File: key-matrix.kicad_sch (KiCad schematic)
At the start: 210 parts, among them SW1 esc, SW10 f9, SW100 R ctrl, SW101 Left, SW102 down, SW103 right, SW104 num zero, SW105 num full stop, SW11 f10, SW12 f11, SW13 f12, SW14 prtscr, SW15 scrlck, SW16 pause, SW17 tilde, SW18 1, SW19 2, SW2 f1, SW20 3, SW21 4, SW22 5, SW23 6, SW24 7, SW25 8, SW26 9, SW27 0, SW28 minus, SW29 equals, SW3 f2, SW30 backspace, SW31 insert, SW32 home, SW33 pgup, SW34 num lock, SW35 num slash, SW36 num mult, SW37 num minus, SW38 tab, SW39 q, SW4 f3, SW40 w, SW41 e, SW42 r, SW43 t, SW44 y, SW45 u, SW46 i, SW47 o, SW48 p, SW49 L brac, SW5 f4, SW50 R brac, SW51 enter, SW52 delete, SW53 end, SW54 pgdn, SW55 num 7, SW56 num 8, SW57 num 9, SW58 num add, SW59 capslock, SW6 f5, SW60 a, SW61 s, SW62 d, SW63 f, SW64 g, SW65 h, SW66 j, SW67 k, SW68 l, SW69 sem colon, SW7 f6, SW70 quote, SW71 tilde, SW72 num 4, SW73 num 5, SW74 num 6, SW75 L shift, SW76 backslash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

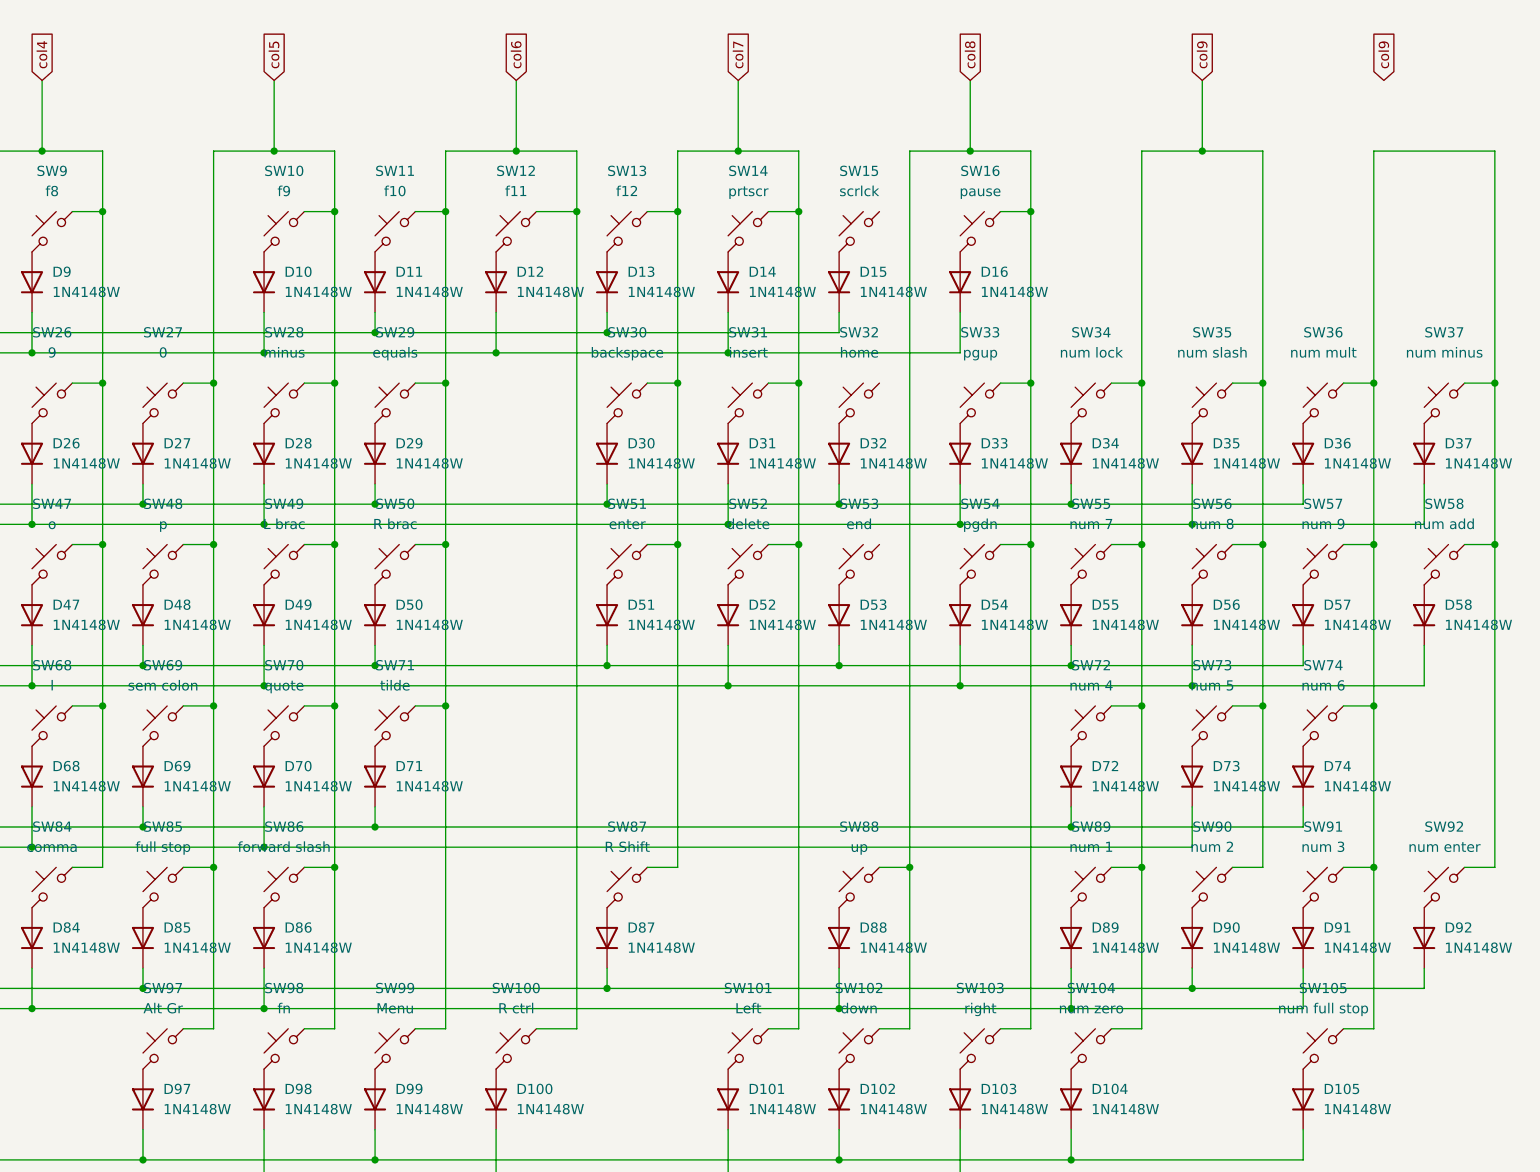
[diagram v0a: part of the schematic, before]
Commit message: Fixed key matrix, laid out LED matrix, started laying out microcontroller
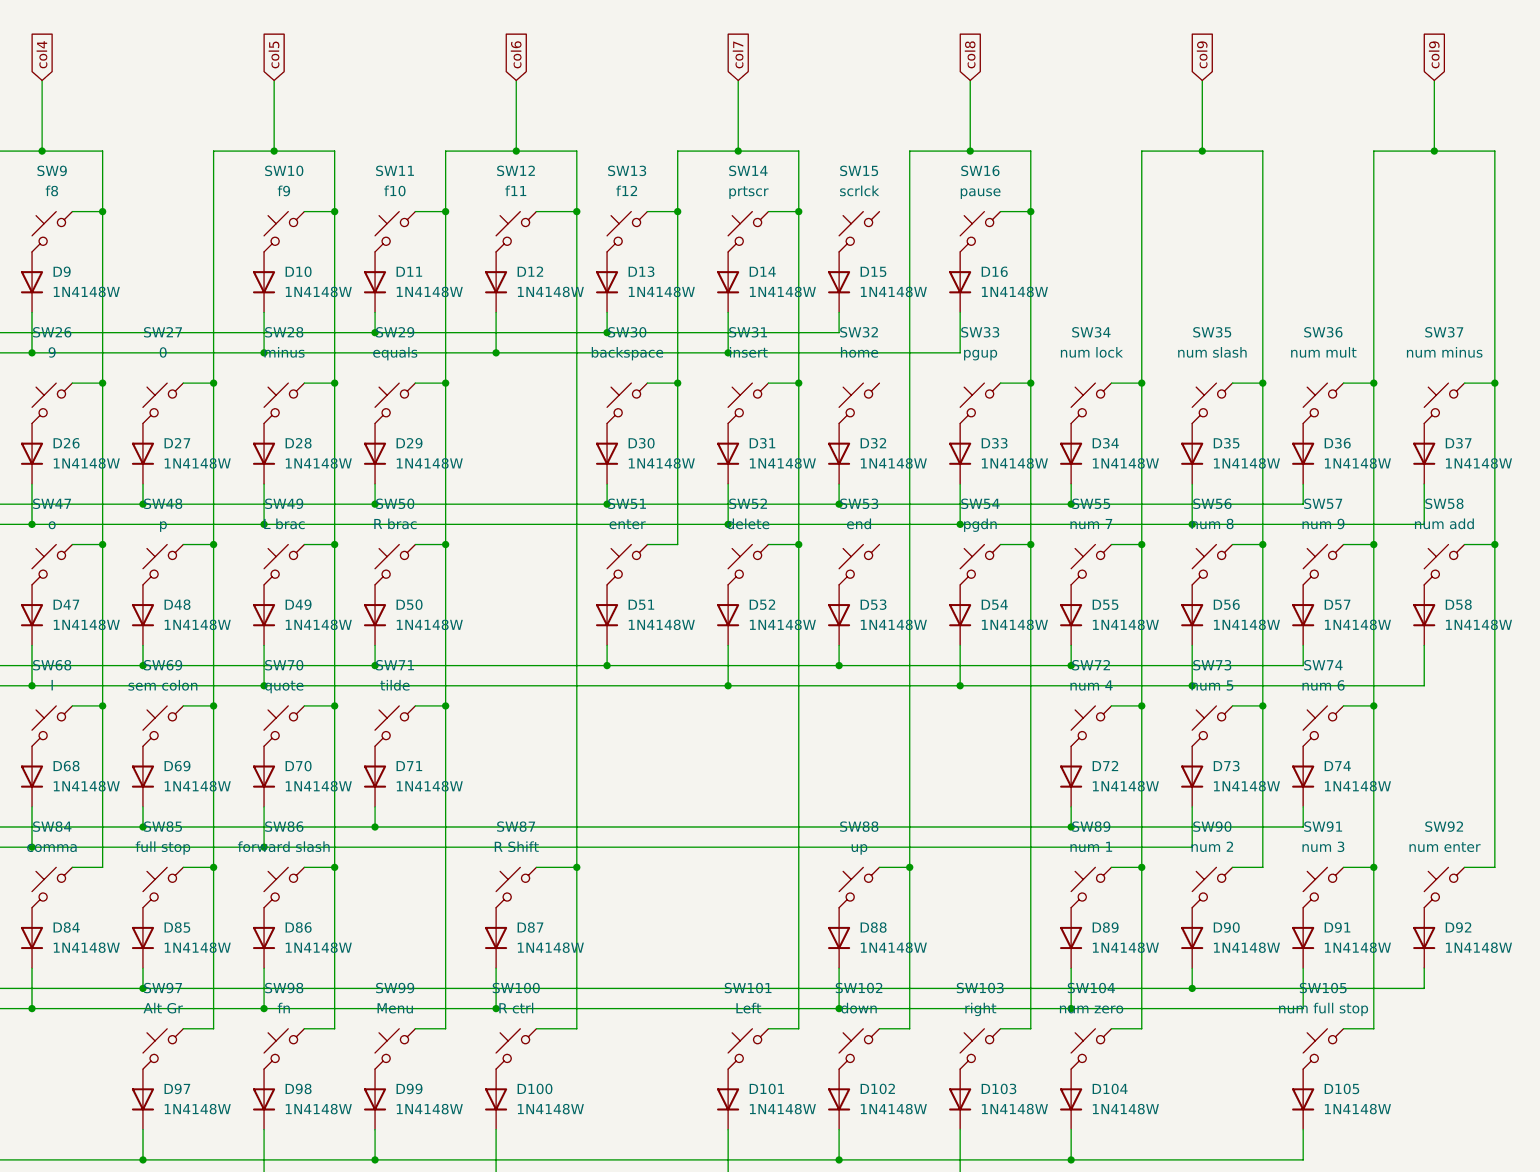
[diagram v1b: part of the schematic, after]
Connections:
- net col6: now also SW87.1
- net col7: no longer SW87.1
- net col9: now also SW105.1, SW36.1, SW37.1, SW57.1, SW58.1, SW74.1, SW91.1, SW92.1
- net row8: no longer D87.1 (K)
- net row9: now also D87.1 (K)
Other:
- moved on the sheet: D87, SW87
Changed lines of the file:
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@@
 	)
 	(junction
+		(at 257.81 134.62)
+		(diameter 0)
+		(color 0 0 0 0)
+	)
+	(junction
 		(at 139.7 114.3)
 		(diameter 0)
@@
 	)
 	(junction
-		(at 270.51 93.98)
+		(at 250.19 44.45)
 		(diameter 0)
 		(color 0 0 0 0)
 	)
 	(junction
-		(at 250.19 44.45)
+		(at 365.76 44.45)
 		(diameter 0)
 		(color 0 0 0 0)
@@
 	)
 	(junction
-		(at 261.62 149.86)
-		(diameter 0)
-		(color 0 0 0 0)
-	)
-	(junction
 		(at 320.04 109.22)
 		(diameter 0)
@@
 	)
 	(junction
+		(at 247.65 152.4)
+		(diameter 0)
+		(color 0 0 0 0)
+	)
+	(junction
 		(at 314.96 93.98)
 		(diameter 0)
@@
 	(wire
 		(pts
-			(xy 266.7 134.62) (xy 270.51 134.62)
-		)
-		(stroke
-			(width 0)
-			(type default)
-		)
-	)
-	(wire
-		(pts
 			(xy 124.46 93.98) (xy 124.46 73.66)
 		)
@@
 	(wire
 		(pts
-			(xy 257.81 52.07) (xy 257.81 154.94)
+			(xy 257.81 52.07) (xy 257.81 134.62)
 		)
 		(stroke
@@
 	(wire
 		(pts
-			(xy 261.62 149.86) (xy 335.28 149.86)
+			(xy 257.81 44.45) (xy 257.81 52.07)
 		)
 		(stroke
@@
 	(wire
 		(pts
-			(xy 257.81 44.45) (xy 257.81 52.07)
+			(xy 369.57 93.98) (xy 373.38 93.98)
 		)
 		(stroke
@@
 	(wire
 		(pts
-			(xy 369.57 93.98) (xy 373.38 93.98)
+			(xy 276.86 64.77) (xy 276.86 69.85)
 		)
 		(stroke
@@
 	(wire
 		(pts
-			(xy 276.86 64.77) (xy 276.86 69.85)
+			(xy 173.99 149.86) (xy 203.2 149.86)
 		)
 		(stroke
@@
 	(wire
 		(pts
-			(xy 173.99 149.86) (xy 203.2 149.86)
+			(xy 144.78 67.31) (xy 173.99 67.31)
 		)
 		(stroke
@@
 	(wire
 		(pts
-			(xy 144.78 67.31) (xy 173.99 67.31)
+			(xy 139.7 93.98) (xy 139.7 114.3)
 		)
 		(stroke
@@
 	(wire
 		(pts
-			(xy 139.7 93.98) (xy 139.7 114.3)
+			(xy 86.36 109.22) (xy 86.36 106.68)
 		)
 		(stroke
@@
 	(wire
 		(pts
-			(xy 86.36 109.22) (xy 86.36 106.68)
+			(xy 365.76 44.45) (xy 373.38 44.45)
 		)
 		(stroke
@@
 	(wire
 		(pts
-			(xy 203.2 149.86) (xy 261.62 149.86)
+			(xy 203.2 149.86) (xy 335.28 149.86)
 		)
 		(stroke
@@
 	(wire
 		(pts
+			(xy 257.81 134.62) (xy 257.81 154.94)
+		)
+		(stroke
+			(width 0)
+			(type default)
+		)
+	)
+	(wire
+		(pts
 			(xy 358.14 93.98) (xy 358.14 73.66)
 		)
@@
 	(wire
 		(pts
+			(xy 252.73 134.62) (xy 257.81 134.62)
+		)
+		(stroke
+			(width 0)
+			(type default)
+		)
+	)
+	(wire
+		(pts
 			(xy 139.7 73.66) (xy 139.7 93.98)
 		)
@@
 	(wire
 		(pts
+			(xy 247.65 152.4) (xy 290.83 152.4)
+		)
+		(stroke
+			(width 0)
+			(type default)
+		)
+	)
+	(wire
+		(pts
 			(xy 153.67 114.3) (xy 153.67 134.62)
 		)
@@
 	(wire
 		(pts
-			(xy 358.14 44.45) (xy 373.38 44.45)
+			(xy 358.14 44.45) (xy 365.76 44.45)
 		)
 		(stroke
@@
 	(wire
 		(pts
-			(xy 261.62 147.32) (xy 261.62 149.86)
-		)
-		(stroke
-			(width 0)
-			(type default)
-		)
-	)
-	(wire
-		(pts
 			(xy 218.44 173.99) (xy 247.65 173.99)
 		)
@@
 	(wire
 		(pts
-			(xy 218.44 152.4) (xy 290.83 152.4)
+			(xy 218.44 152.4) (xy 247.65 152.4)
 		)
 		(stroke
@@
 	(wire
 		(pts
+			(xy 365.76 35.56) (xy 365.76 44.45)
+		)
+		(stroke
+			(width 0)
+			(type default)
+		)
+	)
+	(wire
+		(pts
 			(xy 335.28 86.36) (xy 335.28 91.44)
 		)
@@
 	(wire
 		(pts
+			(xy 247.65 147.32) (xy 247.65 152.4)
+		)
+		(stroke
+			(width 0)
+			(type default)
+		)
+	)
+	(wire
+		(pts
 			(xy 314.96 52.07) (xy 314.96 73.66)
 		)
@@
 	(wire
 		(pts
-			(xy 270.51 134.62) (xy 270.51 93.98)
-		)
-		(stroke
-			(width 0)
-			(type default)
-		)
-	)
-	(wire
-		(pts
 			(xy 62.23 73.66) (xy 66.04 73.66)
 		)
@@
 	(global_label "col9"
 		(shape input)
-		(at 359.41 35.56 90)
+		(at 365.76 35.56 90)
 		(fields_autoplaced yes)
 		(effects
@@
 		)
 		(property "Intersheetrefs" "${INTERSHEET_REFS}"
-			(at 359.41 28.4625 90)
+			(at 365.76 28.4625 90)
 			(effects
 				(font
@@
 	(symbol
 		(lib_id "Switch:SW_Push_45deg")
-		(at 264.16 137.16 0)
+		(at 250.19 137.16 0)
 		(mirror y)
 		(unit 1)
@@
 		(fields_autoplaced yes)
 		(property "Reference" "SW87"
-			(at 264.16 129.54 0)
+			(at 250.19 129.54 0)
 			(effects
 				(font
@@
 		)
 		(property "Value" "R Shift"
-			(at 264.16 132.08 0)
+			(at 250.19 132.08 0)
 			(effects
 				(font
@@
 		)
 		(property "Footprint" "PCM_Switch_Keyboard_Hotswap_Kailh:SW_Hotswap_Kailh_Choc_V1V2_2.75u"
-			(at 264.16 137.16 0)
+			(at 250.19 137.16 0)
 			(effects
 				(font
@@
 		)
 		(property "Datasheet" "~"
-			(at 264.16 137.16 0)
+			(at 250.19 137.16 0)
 			(effects
 				(font
@@
 		)
 		(property "Description" "Push button switch, normally open, two pins, 45° tilted"
-			(at 264.16 137.16 0)
+			(at 250.19 137.16 0)
 			(effects
 				(font
@@
 	(symbol
 		(lib_id "Diode:1N4148WT")
-		(at 261.62 143.51 90)
+		(at 247.65 143.51 90)
 		(unit 1)
 		(exclude_from_sim no)
@@
 		(fields_autoplaced yes)
 		(property "Reference" "D87"
-			(at 264.16 142.2399 90)
+			(at 250.19 142.2399 90)
 			(effects
 				(font
@@
 		)
 		(property "Value" "1N4148W"
-			(at 264.16 144.7799 90)
+			(at 250.19 144.7799 90)
 			(effects
 				(font
@@
 		)
 		(property "Footprint" "Diode_SMD:D_SOD-123"
-			(at 266.065 143.51 0)
+			(at 252.095 143.51 0)
 			(effects
 				(font
@@
 		)
 		(property "Datasheet" "https://www.diodes.com/assets/Datasheets/ds30396.pdf"
-			(at 261.62 143.51 0)
+			(at 247.65 143.51 0)
 			(effects
 				(font
@@
 		)
 		(property "Description" "75V 0.15A Fast switching Diode, SOD-523"
-			(at 261.62 143.51 0)
+			(at 247.65 143.51 0)
 			(effects
 				(font
@@
 		)
 		(property "Sim.Device" "D"
-			(at 261.62 143.51 0)
+			(at 247.65 143.51 0)
 			(effects
 				(font
@@
 		)
 		(property "Sim.Pins" "1=K 2=A"
-			(at 261.62 143.51 0)
+			(at 247.65 143.51 0)
 			(effects
 				(font

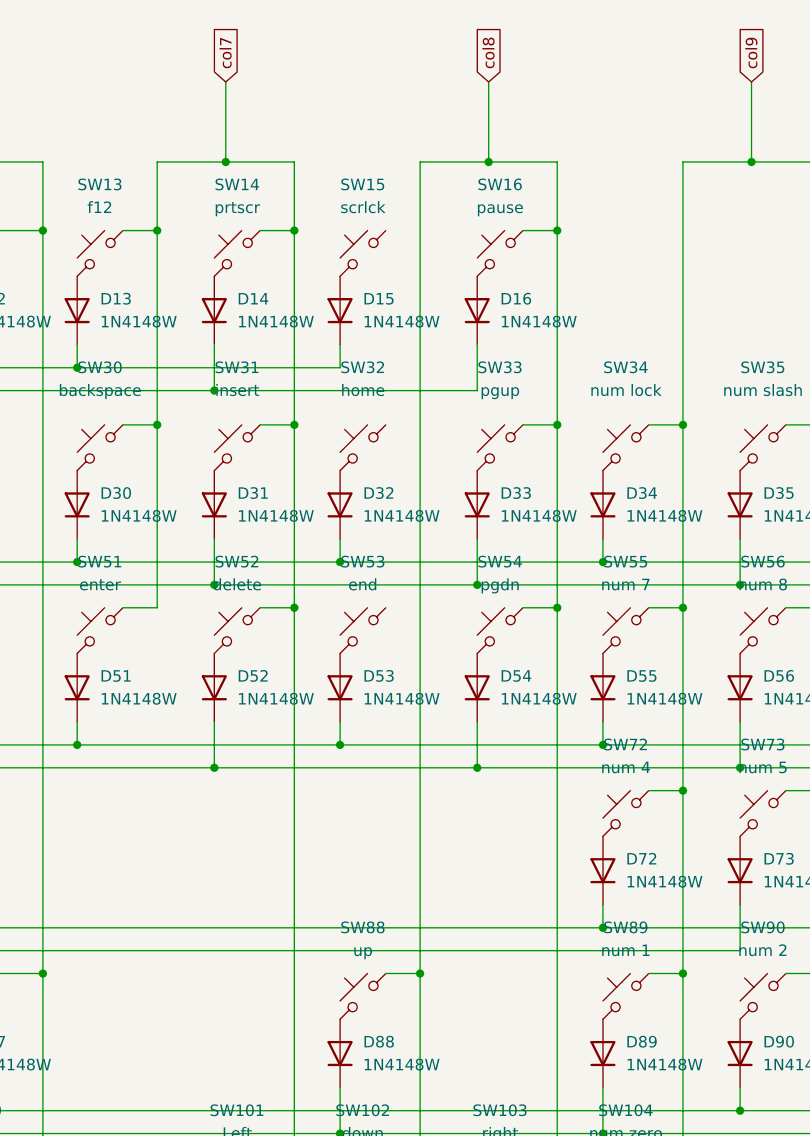
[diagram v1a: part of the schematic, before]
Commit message: Routed microcontroller
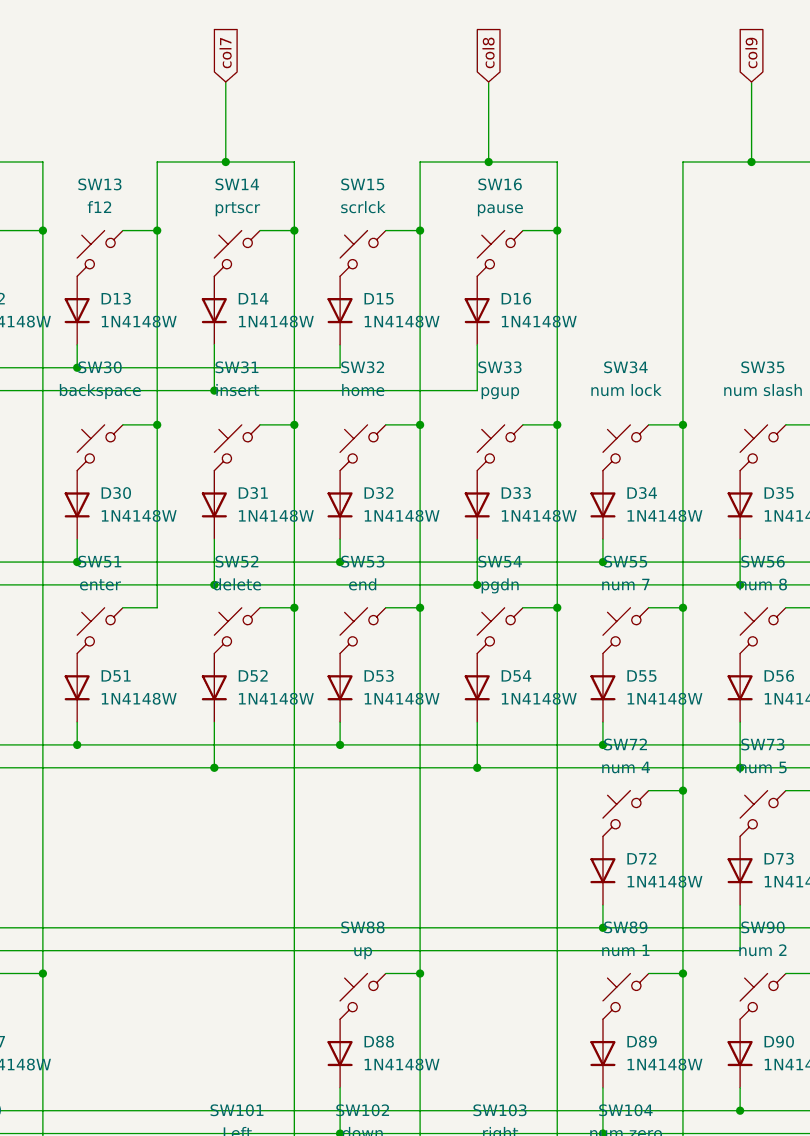
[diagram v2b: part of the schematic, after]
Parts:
- SW1, SW10, SW100, SW101, SW102, SW103, SW104, SW105, SW11, SW12, SW13, SW14, SW15, SW16, SW17, SW18, SW19, SW2, SW20, SW21, SW22, SW23, SW24, SW25, SW26, SW27, SW28, SW29, SW3, SW31, SW32, SW33, SW34, SW35, SW36, SW37, SW39, SW4, SW40, SW41, SW42, SW43, SW44, SW45, SW46, SW47, SW48, SW49, SW5, SW50, SW52, SW53, SW54, SW55, SW56, SW57, SW6, SW60, SW61, SW62, SW63, SW64, SW65, SW66, SW67, SW68, SW69, SW7, SW70, SW71, SW72, SW73, SW74, SW76, SW77, SW78, SW79, SW8, SW80, SW81, SW82, SW83, SW84, SW85, SW86, SW88, SW89, SW9, SW90, SW91, SW93, SW94, SW95, SW97, SW98, SW99: footprint PCM_Switch_Keyboard_Hotswap_Kailh:SW_Hotswap_Kailh_Choc_V1V2_1.00u -> Gateron_KS33_Hotswap:Gateron-KS33-Hotswap-1U
- SW30: footprint PCM_Switch_Keyboard_Hotswap_Kailh:SW_Hotswap_Kailh_Choc_V1V2_2.00u -> Gateron_KS33_Hotswap:Gateron-KS33-Hotswap-2U
- SW38: footprint PCM_Switch_Keyboard_Hotswap_Kailh:SW_Hotswap_Kailh_Choc_V1V2_1.50u -> Gateron_KS33_Hotswap:Gateron-KS33-Hotswap-1.5U
- SW51, SW58, SW92: footprint PCM_Switch_Keyboard_Hotswap_Kailh:SW_Hotswap_Kailh_Choc_V1V2_2.00u_90deg -> Gateron_KS33_Hotswap:Gateron-KS33-Hotswap-2U-90-Deg
- SW59: footprint PCM_Switch_Keyboard_Hotswap_Kailh:SW_Hotswap_Kailh_Choc_V1V2_1.75u -> Gateron_KS33_Hotswap:Gateron-KS33-Hotswap-1.75U
- SW75: footprint PCM_Switch_Keyboard_Hotswap_Kailh:SW_Hotswap_Kailh_Choc_V1V2_1.25u -> Gateron_KS33_Hotswap:Gateron-KS33-Hotswap-1.25U
- SW87: footprint PCM_Switch_Keyboard_Hotswap_Kailh:SW_Hotswap_Kailh_Choc_V1V2_2.75u -> Gateron_KS33_Hotswap:Gateron-KS33-Hotswap-2.75U
- SW96: footprint PCM_Switch_Keyboard_Hotswap_Kailh:SW_Hotswap_Kailh_Choc_V1V2_6.25u -> Gateron_KS33_Hotswap:Gateron-KS33-Hotswap-6.25U
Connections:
- net col8: now also SW15.1, SW32.1, SW53.1
